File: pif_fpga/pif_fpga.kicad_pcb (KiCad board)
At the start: 2 copper layers, 35 x 41 mm, 61 parts, among them P1 CONN_02X20, P2 CONN_01X18, P3 CONN_01X06, P4 CONN_01X05, U1 Si5351A, U2 LCMXO2-2000HC, U3 STM32F070CBT6, U4 W25Q128JVPIQ, U5 74LVC1G14, Y1 25 MHz

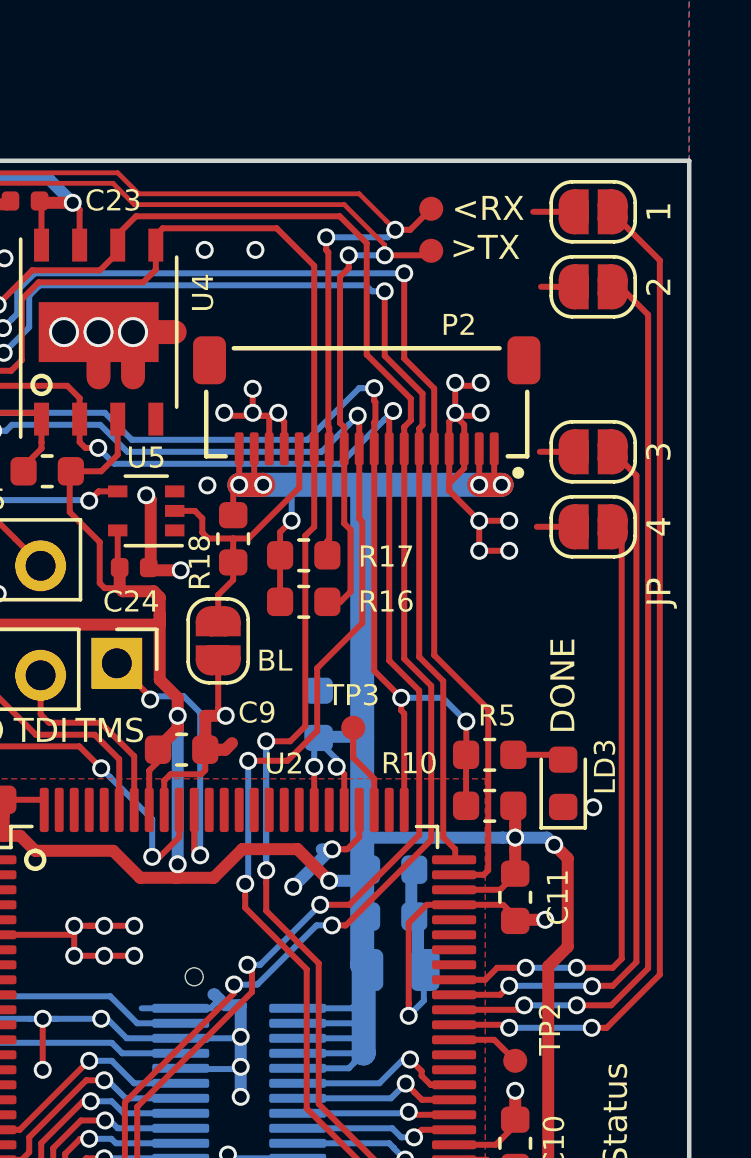
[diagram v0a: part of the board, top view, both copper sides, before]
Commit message: - moved jumpers a bit downwards - no cupper fill under P2
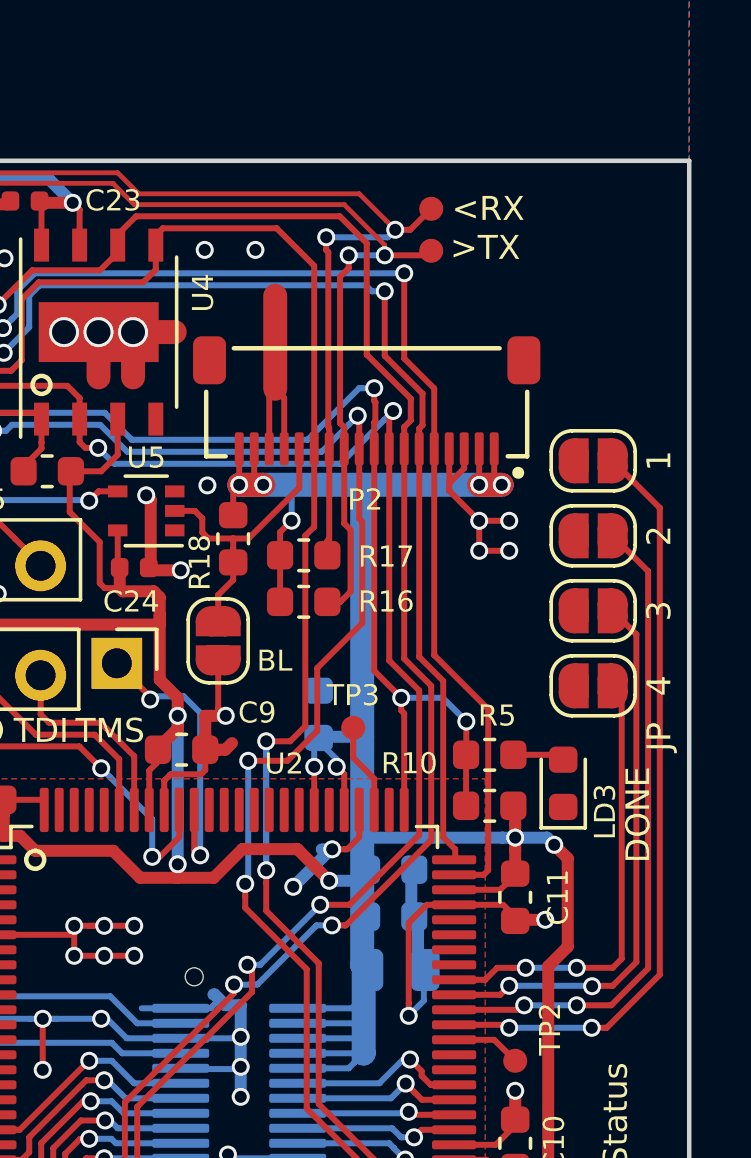
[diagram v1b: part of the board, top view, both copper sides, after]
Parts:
- moved JP1 8.30 mm to (176.8, 109.0)
- moved JP2 8.30 mm to (176.8, 111.5)
- moved JP3 5.30 mm to (176.8, 114.0)
- moved JP4 5.30 mm to (176.8, 116.5)
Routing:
- net /FPGA/JP2: track 30.7 -> 21.9 mm
- net GND: track 192.5 -> 183.8 mm, vias 85 -> 76
- net /FPGA/JP1: track 33.8 -> 25.4 mm
- net /FPGA/JP4: track 20.4 -> 15.1 mm
- net /FPGA/JP3: track 23.8 -> 18.5 mm

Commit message: removed unnecessary via from power rail
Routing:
- net +3V3: track 277.6 -> 279.0 mm, vias 19 -> 18
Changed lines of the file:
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@@
     (thickness 1.6)
     (drawings 45)
-    (tracks 1205)
+    (tracks 1206)
     (zones 0)
     (modules 61)
@@
   )
   (setup
-    (last_trace_width 0.2)
+    (last_trace_width 0.4)
     (user_trace_width 0.16)
     (user_trace_width 0.4)
@@
   (segment (start 154.0575 121.3375) (end 154.22 121.5) (width 0.4) (layer F.Cu) (net 41))
   (segment (start 154.22 121.5) (end 154.95 121.5) (width 0.4) (layer F.Cu) (net 41))
-  (via (at 174.200004 121.56) (size 0.6) (drill 0.4) (layers F.Cu B.Cu) (net 41))
   (segment (start 173.77574 121.56) (end 174.200004 121.56) (width 0.4) (layer B.Cu) (net 41))
   (segment (start 174.200004 121.984264) (end 174.200004 121.56) (width 0.4) (layer F.Cu) (net 41))
@@
   (segment (start 162.35 114.46) (end 162.35 114.14) (width 0.4) (layer F.Cu) (net 41))
   (segment (start 148.22 114.46) (end 162.35 114.46) (width 0.4) (layer F.Cu) (net 41))
+  (segment (start 175.26 121.56) (end 175.5 121.8) (width 0.4) (layer F.Cu) (net 41))
+  (segment (start 174.200004 121.56) (end 175.26 121.56) (width 0.4) (layer F.Cu) (net 41))
   (segment (start 157.59999 104.101466) (end 157.425727 104.275729) (width 0.2) (layer B.Cu) (net 42))
   (segment (start 170.5 102.75) (end 158.184301 102.75) (width 0.2) (layer B.Cu) (net 42))

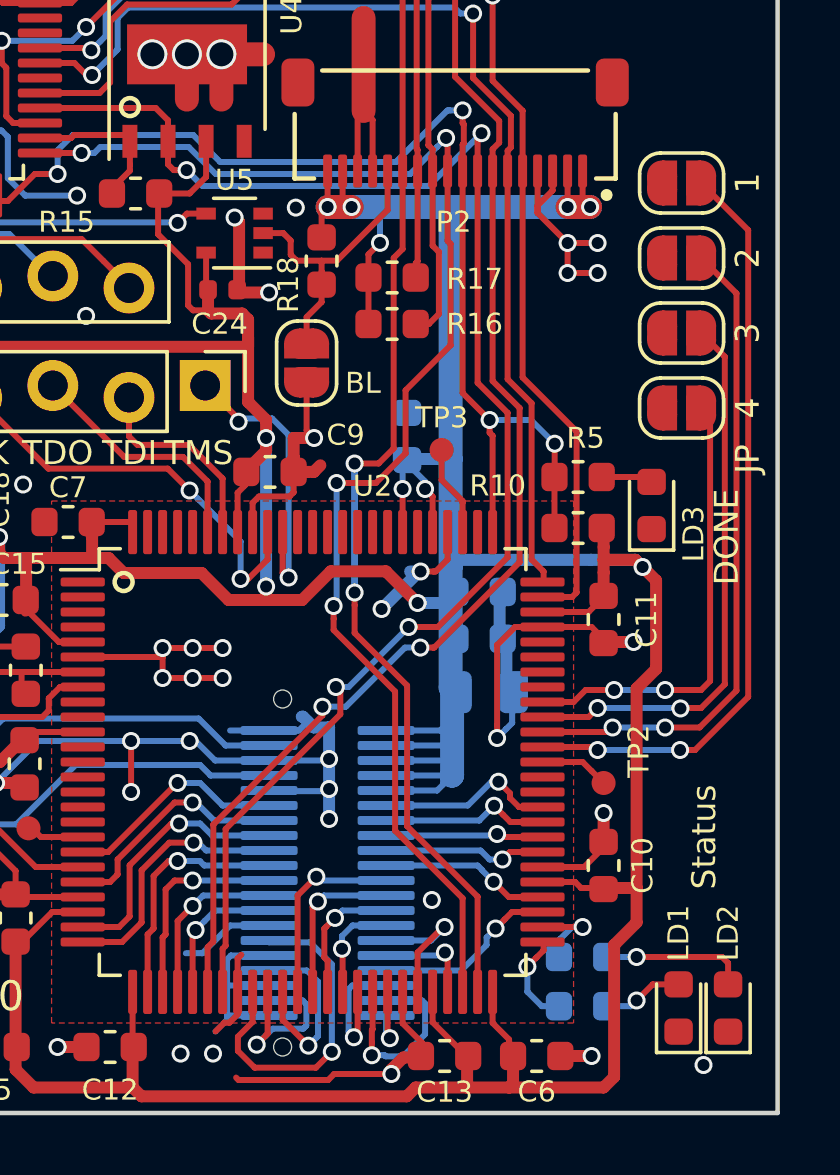
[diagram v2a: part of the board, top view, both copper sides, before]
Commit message: changes some traces under the connector connected solder jumpers to GND
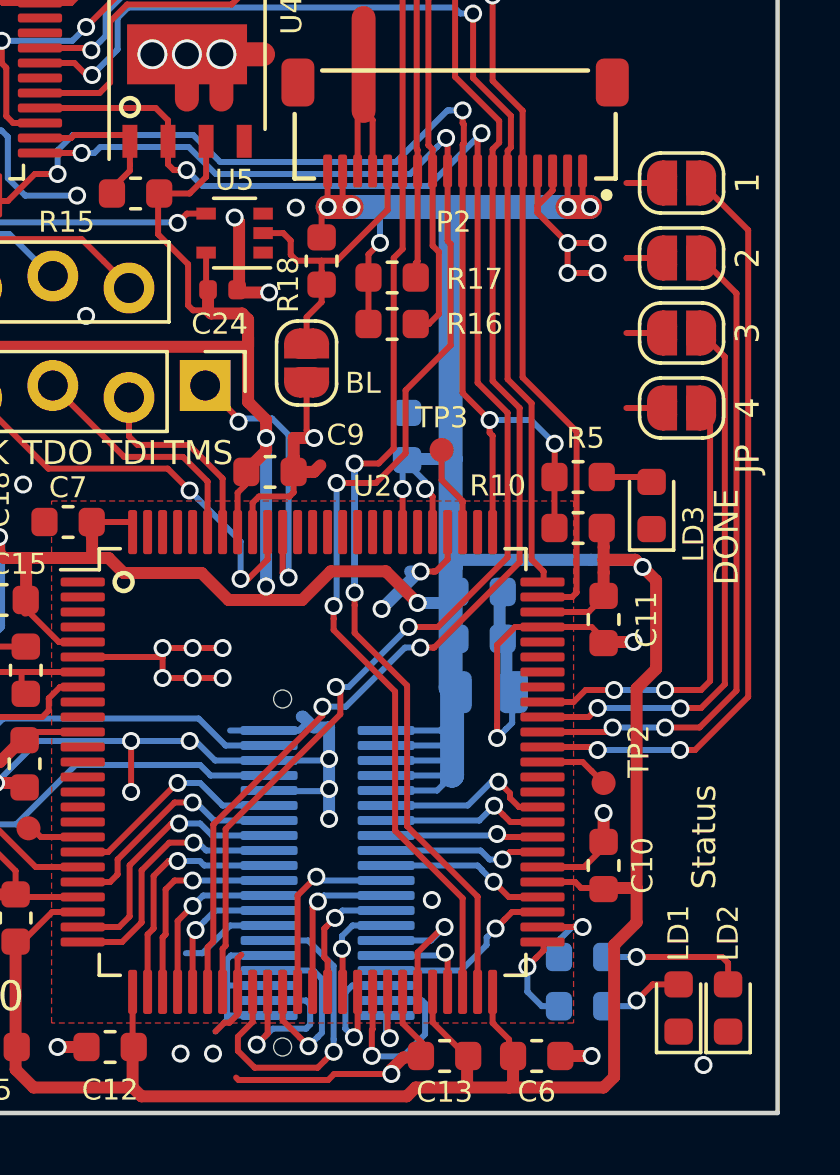
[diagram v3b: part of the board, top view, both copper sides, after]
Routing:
- net GND: track 183.8 -> 188.6 mm
